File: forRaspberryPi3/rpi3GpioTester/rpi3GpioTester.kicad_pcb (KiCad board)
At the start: 2 copper layers, 78.7 x 119.4 mm, 80 parts, among them J1 Raspberry_Pi_2_3, J2 Conn_01x20_Male, J3 Conn_01x12_Male, SW12 SW_Push, SW13 SW_Push, SW16 SW_Push, SW17 SW_Push, SW18 SW_Push, SW19 SW_Push, SW20 SW_Push, SW21 SW_Push, SW22 SW_Push, SW23 SW_Push, SW24 SW_Push, SW25 SW_Push, SW26 SW_Push, SW27 SW_Push, SW4 SW_Push, SW5 SW_Push, SW6 SW_Push

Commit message: rpi3GpioTester 10x10cm design change...
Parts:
- added J_3V32: Conn_01x04_Female, Socket_Strips:Socket_Strip_Straight_1x04_Pitch2.54mm, F.Cu at (101.6, 143.5)
- moved J_GND2 111.7 mm to (101.6, 132.1)
- moved J_5V2 103.0 mm to (101.6, 137.8)
- moved SW12 71.0 mm to (98.4, 91.4)
- moved SW16 71.0 mm to (98.4, 108.0)
- moved SW13 71.0 mm to (98.4, 99.7)
- moved D12 68.9 mm to (90.8, 94.0)
- moved D13 68.9 mm to (90.8, 102.2)
- moved D16 68.9 mm to (90.8, 110.5)
- moved R16 68.9 mm to (95.2, 110.5)
- moved R12 68.9 mm to (95.2, 94.0)
- moved R13 68.9 mm to (95.2, 102.2)
- moved I2C_Grove4 68.2 mm to (128.3, 116.2)
- moved I2C_Grove3 67.7 mm to (128.3, 123.8)
- moved I2C_Grove2 67.2 mm to (128.3, 131.4)
- moved I2C_Grove1 66.7 mm to (128.3, 139.1)
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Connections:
- J_GND2 pad 1: (no net) -> GND
- J_GND2 pad 2: (no net) -> GND
- J_GND2 pad 3: (no net) -> GND
- J_GND2 pad 4: (no net) -> GND
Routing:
- net +3V3: track 615.1 -> 717.3 mm
- net +5V: track 133.7 -> 198.2 mm
- net GND: track 61.5 -> 4.34 mm, vias 3 -> 1
- net G16: track 159.3 -> 201.3 mm, vias 6 -> 7
- net SDA: track 240.0 -> 200.7 mm
- net SCL: track 222.0 -> 193.9 mm
- net G13: track 169.1 -> 188.5 mm, vias 6 -> 8
- net G5: track 162.9 -> 145.3 mm, vias 8 -> 12
- net G6: track 137.5 -> 120.3 mm, vias 6 -> 8
- net G4: track 142.6 -> 128.2 mm, vias 5 -> 6
- net Net-(D5-Pad2): track 31.3 -> 26.0 mm
- net Net-(D4-Pad2): track 18.8 -> 15.2 mm
- net G26: track 67.9 -> 65.9 mm
- net G17: track 117.6 -> 115.9 mm
- net G12: track 182.8 -> 181.5 mm, vias 6 -> 8
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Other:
- board size 78.7 x 119.4 mm -> 99.1 x 99.1 mm
- board text added: "3V3 SDA SCL GND"
- board text added: "PU"
- board text added: "Pull Down"
- board text removed: "GND SCL SDA 3V3"

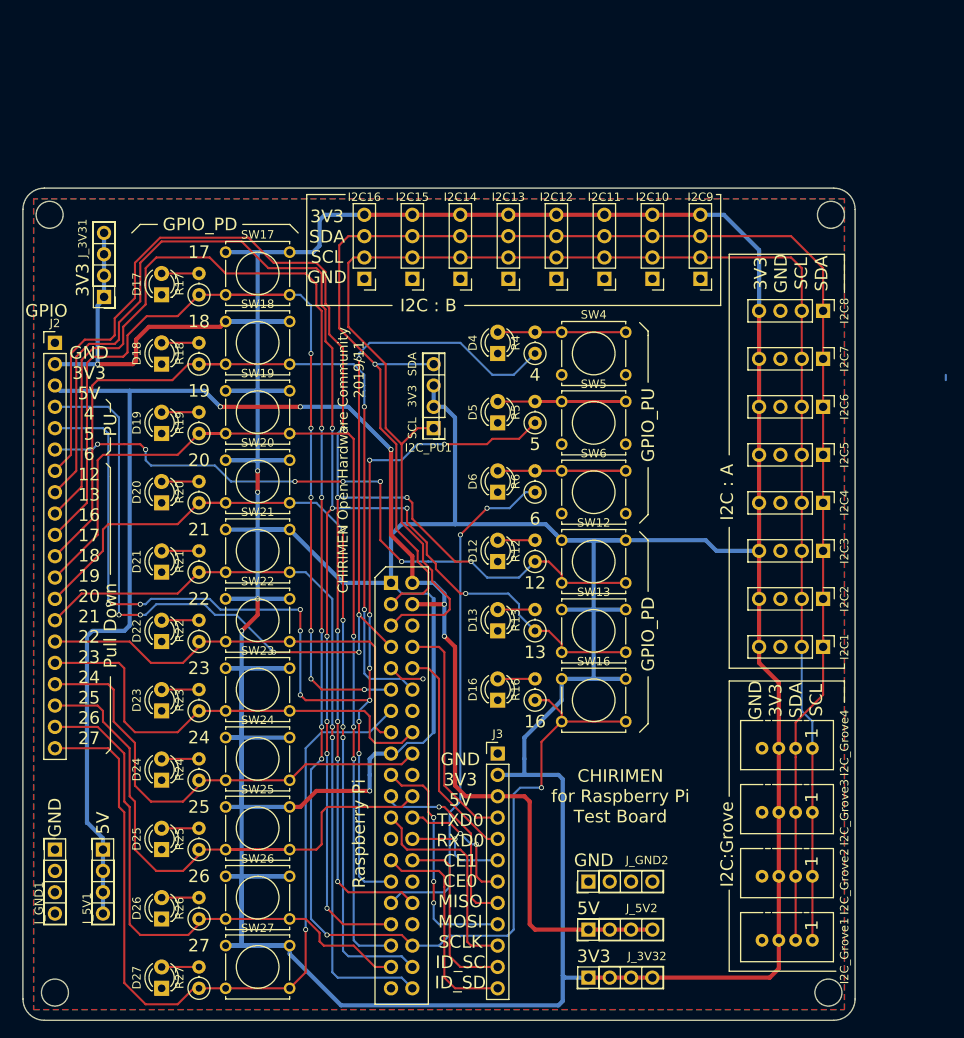
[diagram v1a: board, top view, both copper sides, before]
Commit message: rpi3GpioTester minor change
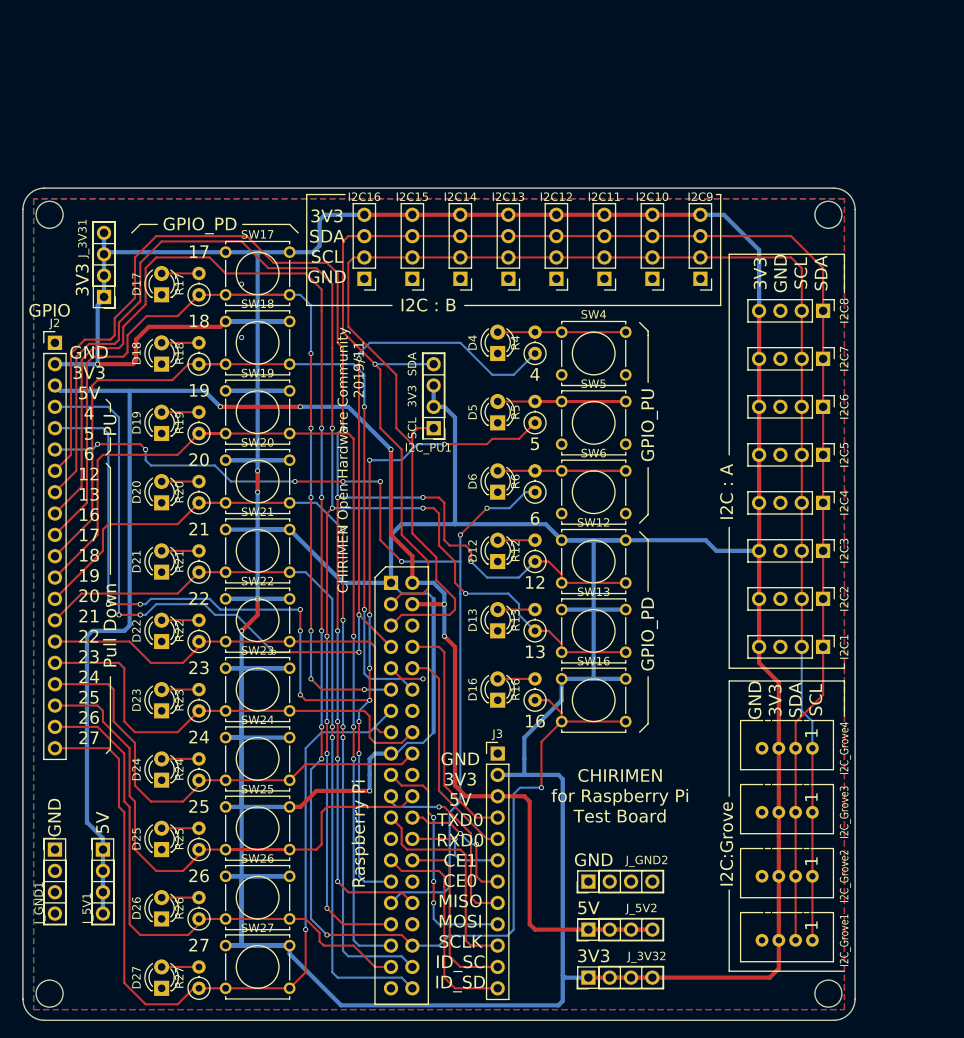
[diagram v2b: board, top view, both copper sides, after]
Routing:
- net +3V3: track 717.3 -> 731.9 mm
- net G12: track 181.5 -> 185.0 mm
- net SDA: track 200.7 -> 199.2 mm
- net G13: track 188.5 -> 190.0 mm
- net (no net): track 0.64 -> 0.00 mm
- net GND: vias 1 -> 3
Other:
- outline, holes or cut-outs redrawn

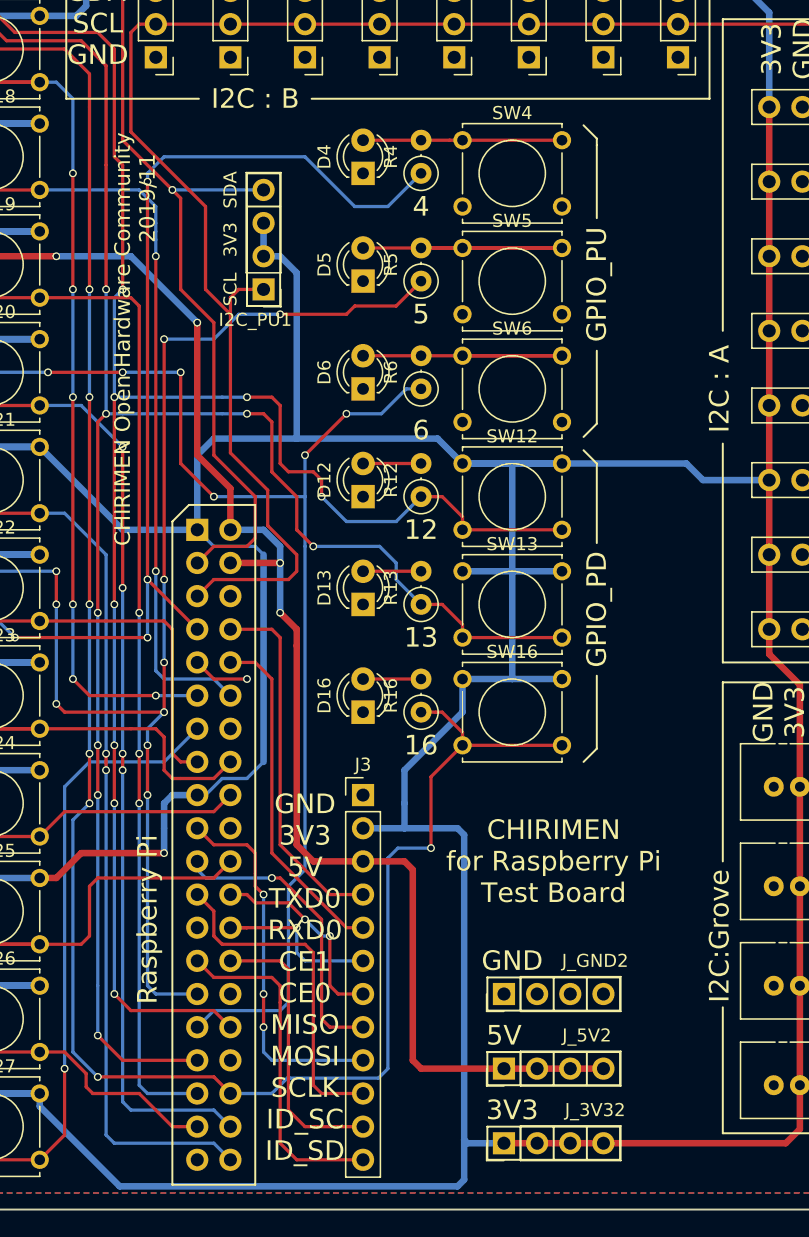
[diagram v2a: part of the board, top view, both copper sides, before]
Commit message: rpiGpioTester silk update
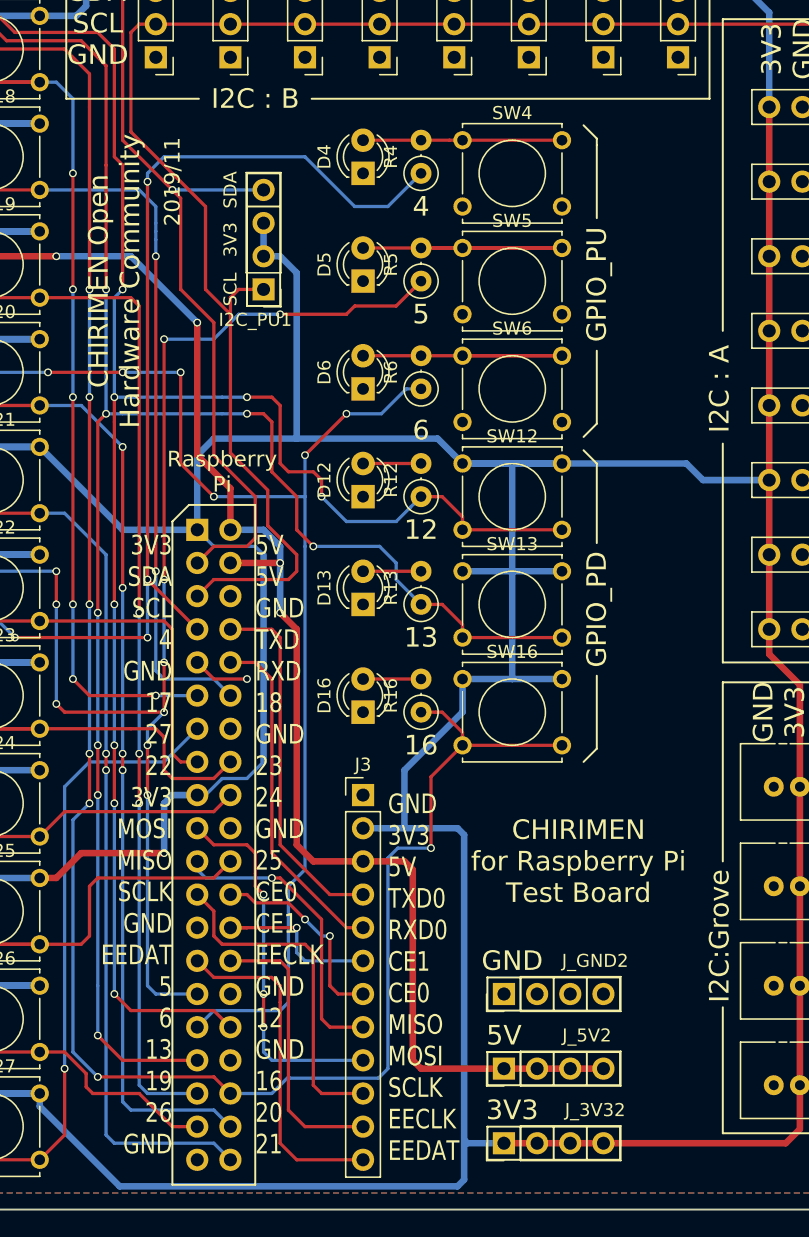
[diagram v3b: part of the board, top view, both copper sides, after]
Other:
- board text added: "3V3 SDA SCL 4 GND 17 27 22 3V3 MOSI MISO SCLK GND EEDAT 5 6 13 19 26 GND"
- board text added: "5V 5V GND TXD RXD 18 GND 23 24 GND 25 CE0 CE1 EECLK GND 12 GND 16 20 21"
- board text added: "GND 3V3 5V TXD0 RXD0 CE1 CE0 MISO MOSI SCLK EECLK EEDAT"
- board text removed: "GND 3V3 5V TXD0 RXD0 CE1 CE0 MISO MOSI SCLK ID_SC ID_SD"
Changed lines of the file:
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@@
   (general
     (thickness 1.6)
-    (drawings 152)
+    (drawings 154)
     (tracks 797)
     (zones 0)
@@
     )
   )
+  (gr_text "5V\n5V\nGND\nTXD\nRXD\n18\nGND\n23\n24\nGND\n25\nCE0\nCE1\nEECLK\nGND\n12\nGND\n16\n20\n21" (at 82.55 120.65) (layer F.SilkS)
+    (effects (font (size 1.5 1.2) (thickness 0.3)) (justify left))
+  )
+  (gr_text "3V3\nSDA\nSCL\n4\nGND\n17\n27\n22\n3V3\nMOSI\nMISO\nSCLK\nGND\nEEDAT\n5\n6\n13\n19\n26\nGND" (at 76.2 120.65) (layer F.SilkS)
+    (effects (font (size 1.5 1.2) (thickness 0.3)) (justify right))
+  )
   (gr_line (start 110.49 144.78) (end 110.49 142.24) (layer F.SilkS) (width 0.15))
   (gr_line (start 107.95 142.24) (end 107.95 144.78) (layer F.SilkS) (width 0.15))
@@
   (gr_arc (start 130.81 146.05) (end 130.81 148.59) (angle -90) (layer Edge.Cuts) (width 0.15))
   (gr_arc (start 130.81 52.07) (end 133.35 52.07) (angle -90) (layer Edge.Cuts) (width 0.15))
-  (gr_text "CHIRIMEN Open Hardware Community" (at 72.39 81.915 90) (layer F.SilkS)
-    (effects (font (size 1.2 1.2) (thickness 0.2)))
+  (gr_text "CHIRIMEN Open\nHardware Community" (at 71.755 77.47 90) (layer F.SilkS)
+    (effects (font (size 1.5 1.5) (thickness 0.3)))
   )
   (gr_circle (center 130.175 52.705) (end 131.699 53.213) (layer Edge.Cuts) (width 0.15))
@@
   (gr_circle (center 37.465 145.415) (end 38.989 145.923) (layer Edge.Cuts) (width 0.15))
   (gr_circle (center 130.175 145.415) (end 131.699 145.923) (layer Edge.Cuts) (width 0.15))
-  (gr_text 2019/11 (at 74.295 71.12 90) (layer F.SilkS)
+  (gr_text 2019/11 (at 76.2 69.85 90) (layer F.SilkS)
     (effects (font (size 1.2 1.2) (thickness 0.2)))
   )
@@
     (effects (font (size 1.5 1.5) (thickness 0.3)))
   )
-  (gr_text "Raspberry Pi" (at 74.295 126.365 90) (layer F.SilkS)
-    (effects (font (size 1.5 1.5) (thickness 0.3)))
+  (gr_text "Raspberry\nPi" (at 80.01 92.075) (layer F.SilkS)
+    (effects (font (size 1.2 1.2) (thickness 0.25)))
   )
   (gr_text GPIO (at 37.465 64.135) (layer F.SilkS)
@@
     (effects (font (size 1.5 1.5) (thickness 0.3)))
   )
-  (gr_text "GND\n3V3\n5V\nTXD0\nRXD0\nCE1\nCE0\nMISO\nMOSI\nSCLK\nID_SC\nID_SD" (at 86.36 130.81) (layer F.SilkS)
-    (effects (font (size 1.5 1.5) (thickness 0.3)))
+  (gr_text "GND\n3V3\n5V\nTXD0\nRXD0\nCE1\nCE0\nMISO\nMOSI\nSCLK\nEECLK\nEEDAT" (at 92.71 130.81) (layer F.SilkS)
+    (effects (font (size 1.5 1.2) (thickness 0.3)) (justify left))
   )
   (gr_text "3V3\nGND\nSCL\nSDA\n" (at 125.73 59.69 90) (layer F.SilkS)
@@
     (effects (font (size 1.5 1.5) (thickness 0.3)))
   )
-  (gr_text "CHIRIMEN\nfor Raspberry Pi\nTest Board" (at 105.41 121.92) (layer F.SilkS)
+  (gr_text "CHIRIMEN\nfor Raspberry Pi\nTest Board" (at 107.315 121.92) (layer F.SilkS)
     (effects (font (size 1.5 1.5) (thickness 0.3)))
   )
